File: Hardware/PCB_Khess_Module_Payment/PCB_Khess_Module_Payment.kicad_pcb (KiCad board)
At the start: 2 copper layers, 84 x 53.8 mm, 24 parts, among them J1 Conn_02x20_Odd_Even, J2 Conn_01x04, J3 Conn_01x08, J5 Conn_01x08

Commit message: feat: improve schematic
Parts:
- added C4: 100µF, Capacitor_SMD:C_0603_1608Metric_Pad1.08x0.95mm_HandSolder, F.Cu at (57.9, 71.3)
- added C5: 100nF, Capacitor_SMD:C_0603_1608Metric_Pad1.08x0.95mm_HandSolder, F.Cu at (57.9, 73.8)
- added C6: 1uF, Capacitor_SMD:C_0603_1608Metric_Pad1.08x0.95mm_HandSolder, F.Cu at (57.9, 76.3)
- added C7: 1u, Capacitor_SMD:C_0603_1608Metric_Pad1.08x0.95mm_HandSolder, F.Cu at (57.9, 78.9)
- added C8: 100n, Capacitor_SMD:C_0603_1608Metric_Pad1.08x0.95mm_HandSolder, F.Cu at (57.9, 81.4)
- added C9: 100n, Capacitor_SMD:C_0603_1608Metric_Pad1.08x0.95mm_HandSolder, F.Cu at (62.3, 71.3)
- added D4: LED Yellow, LED_SMD:LED_0603_1608Metric, F.Cu at (75.2, 76.6)
- added D5: LED_Blue, LED_SMD:LED_0603_1608Metric, F.Cu at (75.2, 79.2)
- added J4: Conn_01x04, Connector_PinHeader_2.54mm:PinHeader_1x04_P2.54mm_Horizontal, F.Cu at (44.7, 86.7)
- added J6: Conn_01x08, Connector_PinHeader_2.54mm:PinHeader_1x08_P2.54mm_Horizontal, F.Cu at (44.7, 64.3)
- added J_Switch1: Conn_01x03, Connector_JST:JST_XA_S03B-XASK-1_1x03_P2.50mm_Horizontal, F.Cu at (59.3, 87.0)
- added L1: 10u, Inductor_SMD:L_0603_1608Metric_Pad1.05x0.95mm_HandSolder, F.Cu at (62.3, 73.8)
- added Q1: RE1C002UNTCL, Package_TO_SOT_SMD:SOT-416, F.Cu at (76.3, 91.0)
- added R10: 4.7k, Resistor_SMD:R_0603_1608Metric_Pad0.98x0.95mm_HandSolder, F.Cu at (66.6, 73.8)
- added R11: 4.7k, Resistor_SMD:R_0603_1608Metric_Pad0.98x0.95mm_HandSolder, F.Cu at (66.6, 76.3)
- added R12: 168K, Resistor_SMD:R_0603_1608Metric_Pad0.98x0.95mm_HandSolder, F.Cu at (66.6, 78.9)
- added R13: 68K, Resistor_SMD:R_0603_1608Metric_Pad0.98x0.95mm_HandSolder, F.Cu at (66.6, 81.4)
- added R14: 10K, Resistor_SMD:R_0603_1608Metric_Pad0.98x0.95mm_HandSolder, F.Cu at (71.0, 71.3)
- added R15: 10K, Resistor_SMD:R_0603_1608Metric_Pad0.98x0.95mm_HandSolder, F.Cu at (71.0, 73.8)
- added R16: 0.1, Resistor_SMD:R_0603_1608Metric_Pad0.98x0.95mm_HandSolder, F.Cu at (71.0, 76.3)
- added R18: 5.1K, Resistor_SMD:R_0603_1608Metric_Pad0.98x0.95mm_HandSolder, F.Cu at (71.0, 78.9)
- added R20: 10K, Resistor_SMD:R_0603_1608Metric_Pad0.98x0.95mm_HandSolder, F.Cu at (71.0, 81.4)
- added R6: 1k7, Resistor_SMD:R_0603_1608Metric_Pad0.98x0.95mm_HandSolder, F.Cu at (62.3, 76.3)
- added R7: R, Resistor_SMD:R_0603_1608Metric_Pad0.98x0.95mm_HandSolder, F.Cu at (62.3, 78.9)
- added R8: 1k, Resistor_SMD:R_0603_1608Metric_Pad0.98x0.95mm_HandSolder, F.Cu at (62.3, 81.4)
- added R9: 10k, Resistor_SMD:R_0603_1608Metric_Pad0.98x0.95mm_HandSolder, F.Cu at (66.6, 71.3)
- added U1: FSV330AF, Diode_SMD:D_SOD-123, F.Cu at (70.7, 84.3)
- added U2: FSV330AF, Diode_SMD:D_SOD-123, F.Cu at (70.7, 87.7)
- added U3: 171013801, Package_DFN_QFN:QFN-16-1EP_3x3mm_P0.5mm_EP1.9x1.9mm, F.Cu at (76.1, 72.7)
- added U4: TP5100, Package_DFN_QFN:QFN-16-1EP_4x4mm_P0.5mm_EP2.45x2.45mm, F.Cu at (71.3, 92.5)
- added U5: USBLC6-2SC6, Package_TO_SOT_SMD:SOT-23-6, F.Cu at (76.1, 85.0)
- C1: value 100µF -> 10u
- C2: value 100nF -> 1u
- C3: value 1uF -> 47u
- J2: value Conn_01x04 -> Conn_01x02; footprint Connector_PinHeader_2.54mm:PinHeader_1x04_P2.54mm_Horizontal -> Connector_JST:JST_XA_S02B-XASK-1_1x02_P2.50mm_Horizontal
- J5: value Conn_01x08 -> USB_C_Receptacle_USB2.0; footprint Connector_PinHeader_2.54mm:PinHeader_1x08_P2.54mm_Horizontal -> Connector_USB:USB_C_Receptacle_HRO_TYPE-C-31-M-12
- R1: value 4.7k -> 5k6
- R17: value 10K -> 5.1K; footprint Resistor_SMD:R_0402_1005Metric -> Resistor_SMD:R_0603_1608Metric_Pad0.98x0.95mm_HandSolder
- R19: footprint Resistor_SMD:R_0402_1005Metric -> Resistor_SMD:R_0603_1608Metric_Pad0.98x0.95mm_HandSolder
- R2: value 4.7k -> 470
- R4: value 470 -> 49k9
- R5: value 10K -> 10k; footprint Resistor_SMD:R_0402_1005Metric -> Resistor_SMD:R_0603_1608Metric_Pad0.98x0.95mm_HandSolder
- moved F1 44.5 mm to (60.4, 64.8), turned to 0 degrees
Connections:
- C1 pad 1: GND -> VCC
- C1 pad 2: +5V_PI -> GND
- C2 pad 1: +5V_PI -> Net-(U3-Vcc)
- C3 pad 1: +3.3V_PI -> 5V_BUCK
- F1 pad 1: +5V_IN -> +5V_PI
- J1 pad 26: unconnected-(J1-Pin_26-Pad26) -> RSTO
- J1 pad 7: unconnected-(J1-Pin_7-Pad7) -> Batterie_Faible_GPIO
- J1 pad 8: unconnected-(J1-Pin_8-Pad8) -> Charge_Batterie_GPIO
- J2 pad 1: +3.3V_PI -> VCC
- J3 pad 1: SCKD -> SCK
- J3 pad 4: MOSID -> MOSI
- R1 pad 1: +3.3V_PI -> Net-(U3-FSW_1)
- R1 pad 2: SDA -> GND
- R17 pad 1: Column3 -> Net-(J5-CC1)
- R19 pad 1: Column4 -> Column3
- R2 pad 1: +3.3V_PI -> +5V_PI
- R2 pad 2: SCL -> Net-(D2-A)
- R3 pad 1: +5V_PI -> +3.3V_PI
- R3 pad 2: Net-(D2-A) -> Net-(D3-A)
- R4 pad 1: +3.3V_PI -> 5V_BUCK
- R4 pad 2: Net-(D3-A) -> Net-(U3-FB)
- R5 pad 1: Column1 -> Net-(U3-FB)
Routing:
- net +5V_PI: track 136.5 -> 89.3 mm
- net +5V_IN: track 12.0 -> 0.00 mm
- net SDA: track 34.7 -> 31.4 mm
- net GND: track 12.1 -> 15.4 mm
- net Net-(D2-A): track 1.92 -> 5.22 mm
- net SCL: track 37.1 -> 33.8 mm
- net Column4: track 36.1 -> 33.1 mm
- net Net-(J5-CC1): track 0.00 -> 3.00 mm
- net Net-(U3-FB): track 0.00 -> 2.99 mm
- net Column1: track 46.8 -> 43.9 mm

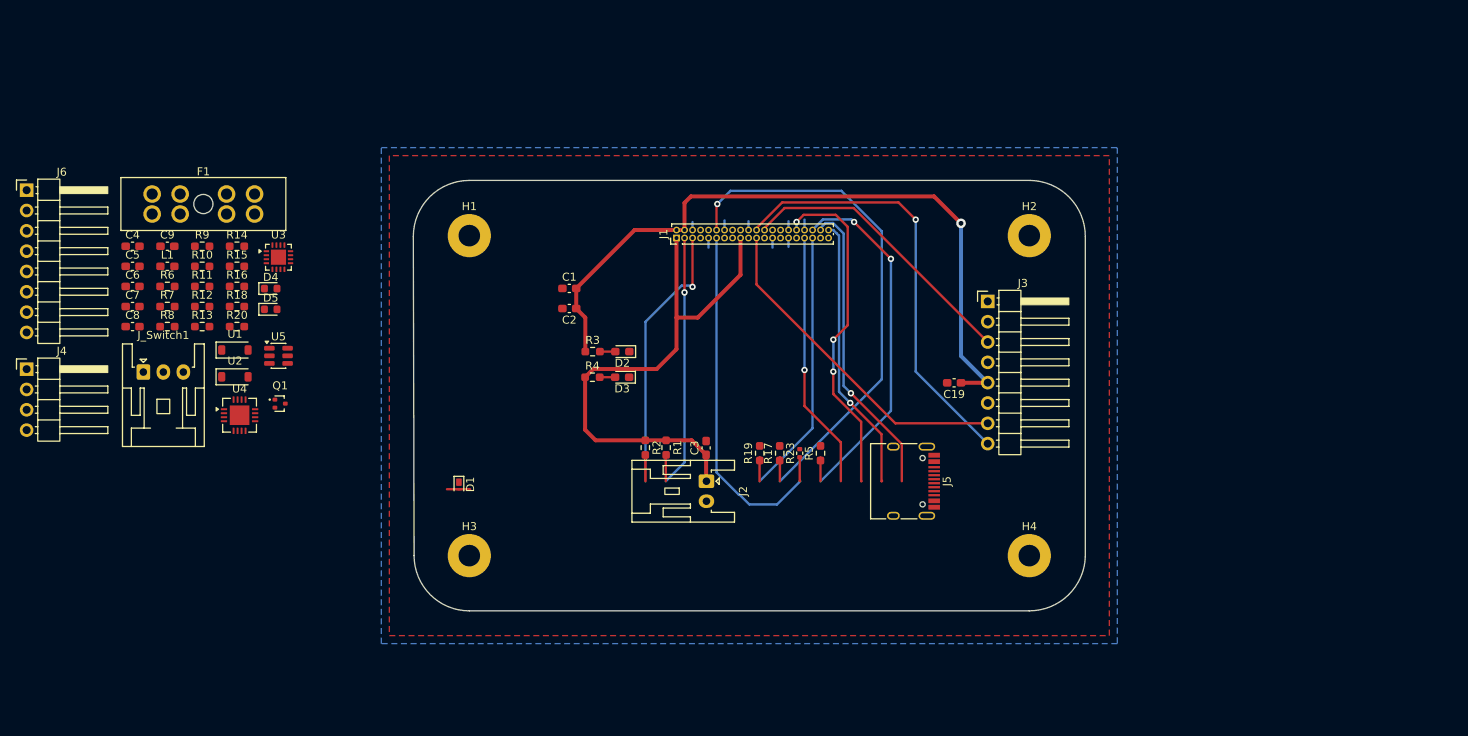
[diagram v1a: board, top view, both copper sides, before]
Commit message: fix: update schematic
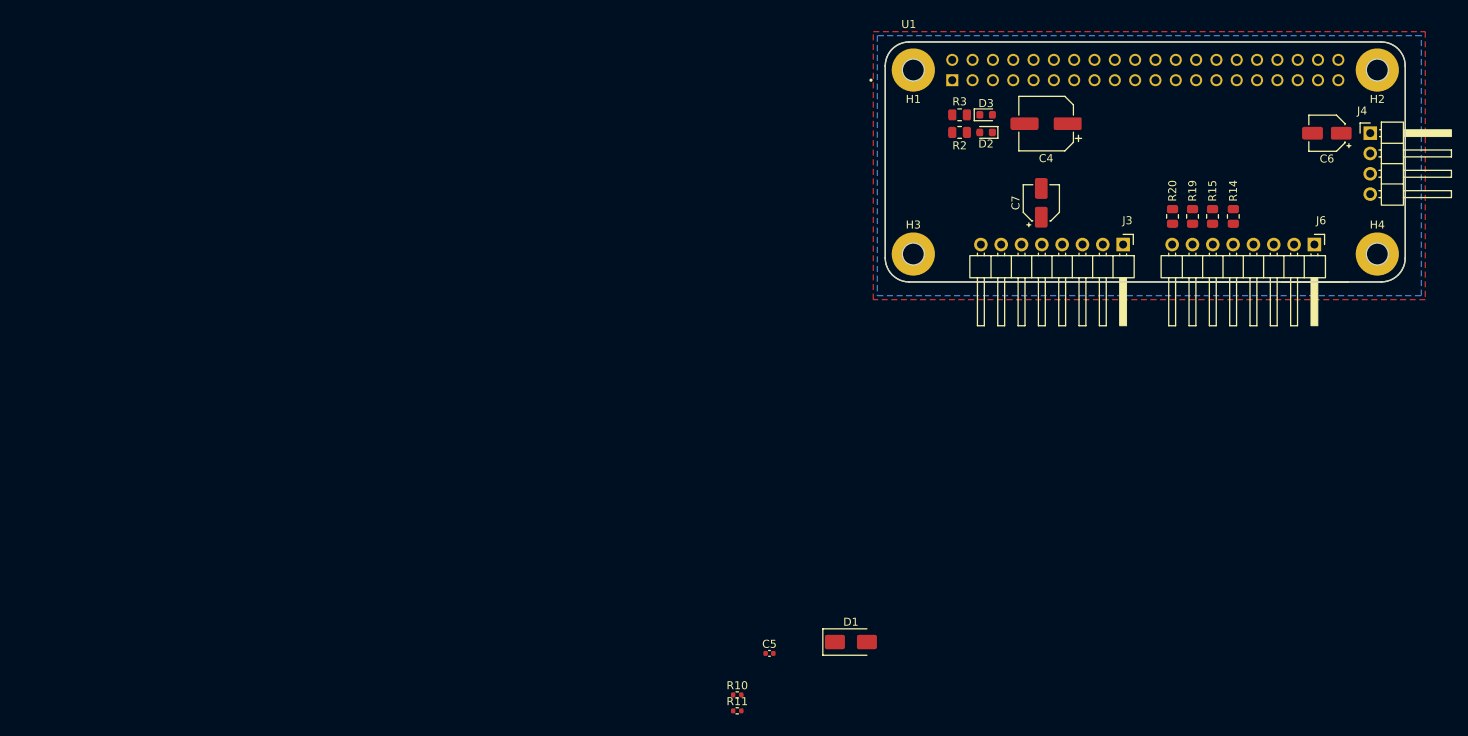
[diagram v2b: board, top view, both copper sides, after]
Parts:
- removed C1: 10u, Capacitor_SMD:C_0603_1608Metric_Pad1.08x0.95mm_HandSolder
- removed C19, C2: 1u, Capacitor_SMD:C_0603_1608Metric_Pad1.08x0.95mm_HandSolder
- removed C3: 47u, Capacitor_SMD:C_0603_1608Metric_Pad1.08x0.95mm_HandSolder
- removed C8, C9: 100n, Capacitor_SMD:C_0603_1608Metric_Pad1.08x0.95mm_HandSolder
- removed D4: LED Yellow, LED_SMD:LED_0603_1608Metric
- removed D5: LED_Blue, LED_SMD:LED_0603_1608Metric
- removed F1: Fuse, Fuse:FuseHolder_Blade_ATO_Littelfuse_FLR_178.6165
- removed J1: Conn_02x20_Odd_Even, Connector_PinHeader_1.00mm:PinHeader_2x20_P1.00mm_Vertical
- removed J2: Conn_01x02, Connector_JST:JST_XA_S02B-XASK-1_1x02_P2.50mm_Horizontal
- removed J5: USB_C_Receptacle_USB2.0, Connector_USB:USB_C_Receptacle_HRO_TYPE-C-31-M-12
- removed J_Switch1: Conn_01x03, Connector_JST:JST_XA_S03B-XASK-1_1x03_P2.50mm_Horizontal
- removed L1: 10u, Inductor_SMD:L_0603_1608Metric_Pad1.05x0.95mm_HandSolder
- removed Q1: RE1C002UNTCL, Package_TO_SOT_SMD:SOT-416
- removed R1: 5k6, Resistor_SMD:R_0603_1608Metric_Pad0.98x0.95mm_HandSolder
- removed R12: 168K, Resistor_SMD:R_0603_1608Metric_Pad0.98x0.95mm_HandSolder
- removed R13: 68K, Resistor_SMD:R_0603_1608Metric_Pad0.98x0.95mm_HandSolder
- removed R16: 0.1, Resistor_SMD:R_0603_1608Metric_Pad0.98x0.95mm_HandSolder
- removed R17, R18: 5.1K, Resistor_SMD:R_0603_1608Metric_Pad0.98x0.95mm_HandSolder
- removed R23: 10K, Resistor_SMD:R_0402_1005Metric
- removed R4: 49k9, Resistor_SMD:R_0603_1608Metric_Pad0.98x0.95mm_HandSolder
- removed R5, R9: 10k, Resistor_SMD:R_0603_1608Metric_Pad0.98x0.95mm_HandSolder
- removed R6: 1k7, Resistor_SMD:R_0603_1608Metric_Pad0.98x0.95mm_HandSolder
- removed R7: R, Resistor_SMD:R_0603_1608Metric_Pad0.98x0.95mm_HandSolder
- removed R8: 1k, Resistor_SMD:R_0603_1608Metric_Pad0.98x0.95mm_HandSolder
- removed U2: FSV330AF, Diode_SMD:D_SOD-123
- removed U3: 171013801, Package_DFN_QFN:QFN-16-1EP_3x3mm_P0.5mm_EP1.9x1.9mm
- removed U4: TP5100, Package_DFN_QFN:QFN-16-1EP_4x4mm_P0.5mm_EP2.45x2.45mm
- removed U5: USBLC6-2SC6, Package_TO_SOT_SMD:SOT-23-6
- C4: value 100µF -> 100u; footprint Capacitor_SMD:C_0603_1608Metric_Pad1.08x0.95mm_HandSolder -> Capacitor_SMD:CP_Elec_6.3x7.7
- C5: value 100nF -> 100n; footprint Capacitor_SMD:C_0603_1608Metric_Pad1.08x0.95mm_HandSolder -> Capacitor_SMD:C_0402_1005Metric
- C6: value 1uF -> 1u; footprint Capacitor_SMD:C_0603_1608Metric_Pad1.08x0.95mm_HandSolder -> Capacitor_SMD:CP_Elec_4x5.4
- C7: footprint Capacitor_SMD:C_0603_1608Metric_Pad1.08x0.95mm_HandSolder -> Capacitor_SMD:CP_Elec_4x5.4
- D1: value PTVS5V0Z1USK -> 824 500 500; footprint Diode_SMD:Nexperia_DSN1608-2_1.6x0.8mm -> Diode_SMD:D_SMA
- D2, D3: footprint LED_SMD:LED_0603_1608Metric_Pad1.05x0.95mm_HandSolder -> LED_SMD:LED_0603_1608Metric
- R10, R11: footprint Resistor_SMD:R_0603_1608Metric_Pad0.98x0.95mm_HandSolder -> Resistor_SMD:R_0402_1005Metric
- R14, R15, R19, R20: value 10K -> 10k; footprint Resistor_SMD:R_0603_1608Metric_Pad0.98x0.95mm_HandSolder -> Resistor_SMD:R_0805_2012Metric
- R2, R3: footprint Resistor_SMD:R_0603_1608Metric_Pad0.98x0.95mm_HandSolder -> Resistor_SMD:R_0805_2012Metric
- U1: value FSV330AF -> RASPBERRY_PI_ZERO_2_W; footprint Diode_SMD:D_SOD-123 -> RASPBERRY_PI_ZERO_2_W:MODULE_RASPBERRY_PI_ZERO_2_W
- moved J4 170.5 mm to (212.6, 57.2)
- moved J6 161.1 mm to (205.6, 71.1), turned to -90 degrees
- moved C6 150.5 mm to (207.2, 57.2), turned to 180 degrees
- moved R14 124.6 mm to (195.5, 67.6), turned to 90 degrees
- moved R15 122.1 mm to (192.9, 67.6), turned to 90 degrees
- moved R20 117.8 mm to (187.9, 67.6), turned to 90 degrees
- moved U1 116.2 mm to (184.5, 60.8)
- moved C4 115.2 mm to (172.1, 56.0), turned to 180 degrees
- moved C7 114.3 mm to (171.5, 65.9), turned to 90 degrees
- moved C5 93.2 mm to (137.5, 122.2)
- moved R10 85.7 mm to (133.5, 127.4)
- moved R11 85.4 mm to (133.5, 129.4)
- moved H3 67.1 mm to (155.5, 72.3)
- moved R19 61.7 mm to (190.4, 67.6)
- moved H1 59.2 mm to (155.5, 49.3), turned to 180 degrees
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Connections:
- J3 pad 2: RSTO -> MISO
- J3 pad 3: SS -> MOSI
- J3 pad 4: MOSI -> SS
- J3 pad 7: MISO -> IRQ
- J3 pad 8: IRQ -> RSTO
- U1 pad 1: Net-(J_Switch1-Pin_1) -> +3.3V_PI
- U1 pad 2: 5V_USB -> +5V_PI
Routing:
- net +5V_PI: track 89.3 -> 0.00 mm, vias 1 -> 0
- net +3.3V_PI: track 68.4 -> 0.00 mm
- net Column3: track 66.1 -> 0.00 mm, vias 1 -> 0
- net IRQ: track 54.1 -> 0.00 mm, vias 1 -> 0
- net Column2: track 45.9 -> 0.00 mm
- net Column1: track 43.9 -> 0.00 mm, vias 2 -> 0
- net ROW3: track 42.4 -> 0.00 mm, vias 3 -> 0
- net MISO: track 41.9 -> 0.00 mm
- net ROW1: track 37.9 -> 0.00 mm, vias 1 -> 0
- net SS: track 36.1 -> 0.00 mm
- net ROW2: track 34.6 -> 0.00 mm, vias 1 -> 0
- net SCL: track 33.8 -> 0.00 mm, vias 1 -> 0
- net Column4: track 33.1 -> 0.00 mm
- net ROW4: track 32.3 -> 0.00 mm, vias 1 -> 0
- net SDA: track 31.4 -> 0.00 mm, vias 1 -> 0
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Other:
- board size 84 x 53.8 mm -> 65 x 30 mm
- copper layers 2 -> 4

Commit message: feat: shield pcb raspberry
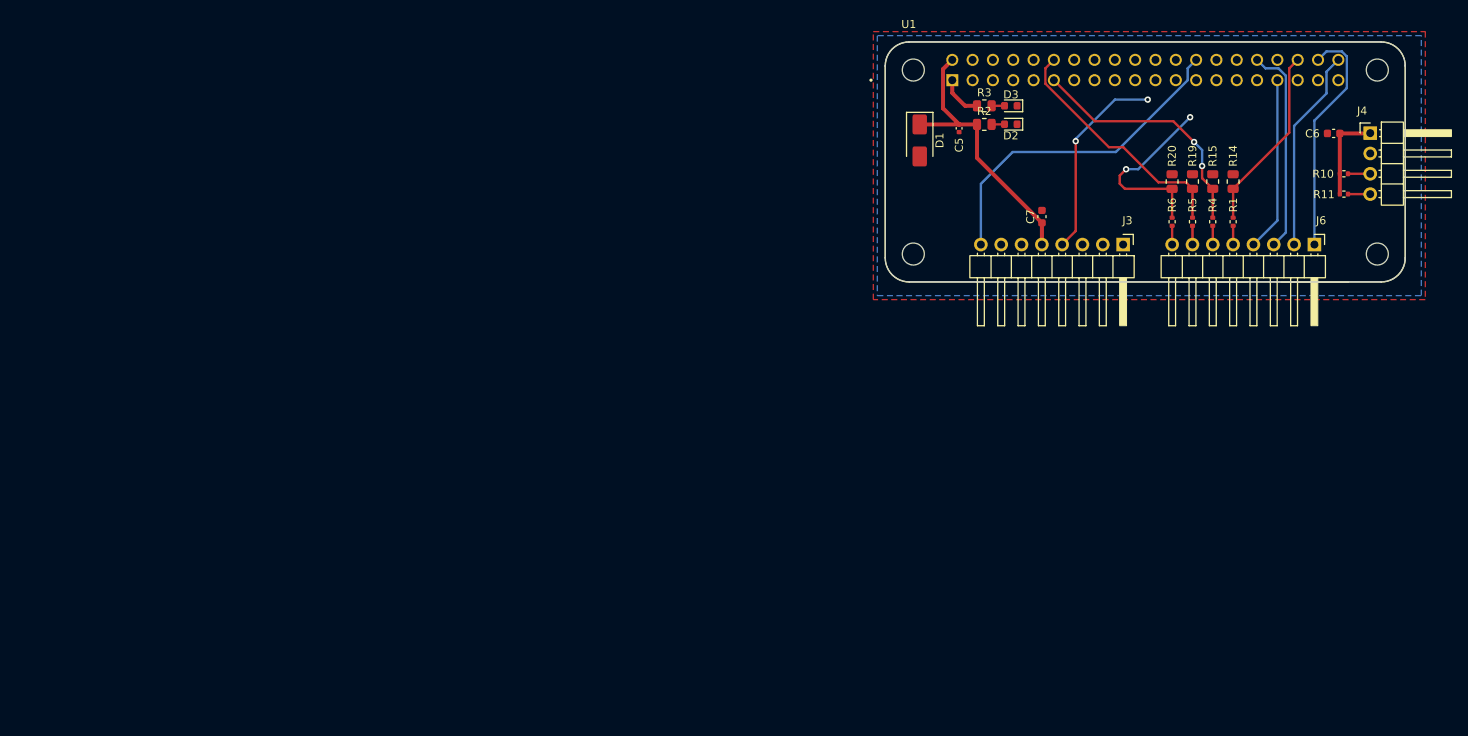
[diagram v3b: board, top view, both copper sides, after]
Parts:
- removed C4: 100u, Capacitor_SMD:CP_Elec_6.3x7.7
- removed H1, H2, H3, H4: MountingHole_Pad, MountingHole:MountingHole_2.7mm_M2.5_Pad
- added R1: 330, Resistor_SMD:R_0402_1005Metric, F.Cu at (195.5, 68.3)
- added R4: 330, Resistor_SMD:R_0402_1005Metric, F.Cu at (192.9, 68.3)
- added R5: 330, Resistor_SMD:R_0402_1005Metric, F.Cu at (190.4, 68.3)
- added R6: 330, Resistor_SMD:R_0402_1005Metric, F.Cu at (187.8, 68.3)
- C6, C7: footprint Capacitor_SMD:CP_Elec_4x5.4 -> Capacitor_SMD:C_0603_1608Metric
- moved R10 100.0 mm to (209.3, 62.3)
- moved R11 99.6 mm to (209.3, 64.8)
- moved C5 69.8 mm to (161.2, 56.6), turned to -90 degrees
- moved D1 63.3 mm to (156.3, 58.1), turned to -90 degrees
- moved R20 4.36 mm to (187.8, 63.2)
- moved R14 4.36 mm to (195.5, 63.2)
- moved R15 4.36 mm to (192.9, 63.2)
- moved R19 4.36 mm to (190.4, 63.2)
- moved D3 3.29 mm to (167.7, 53.8), turned to 180 degrees
- moved R3 3.29 mm to (164.4, 53.8)
- moved D2 3.27 mm to (167.7, 56.1)
- moved R2 3.25 mm to (164.4, 56.1), turned to 0 degrees
- moved C7 1.73 mm to (171.6, 67.6)
- moved C6 0.84 mm to (208.0, 57.2)
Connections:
- J6 pad 5: Column1 -> Net-(J6-Pin_5)
- J6 pad 6: Column2 -> Net-(J6-Pin_6)
- J6 pad 7: Column3 -> Net-(J6-Pin_7)
- J6 pad 8: Column4 -> Net-(J6-Pin_8)
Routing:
- net +3.3V_PI: track 0.00 -> 72.7 mm
- net SCL: track 0.00 -> 59.2 mm
- net SDA: track 0.00 -> 57.3 mm
- net RSTO: track 0.00 -> 41.8 mm
- net Column4: track 0.00 -> 38.6 mm, vias 0 -> 2
- net +5V_PI: track 0.00 -> 37.5 mm
- net SS: track 0.00 -> 32.0 mm, vias 0 -> 2
- net IRQ: track 0.00 -> 31.9 mm
- net Column2: track 0.00 -> 31.1 mm, vias 0 -> 2
- net Column3: track 0.00 -> 30.8 mm
- net ROW1: track 0.00 -> 29.5 mm
- net ROW3: track 0.00 -> 26.1 mm
- net ROW2: track 0.00 -> 25.4 mm
- net SCK: track 0.00 -> 23.3 mm
- net MISO: track 0.00 -> 23.3 mm
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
